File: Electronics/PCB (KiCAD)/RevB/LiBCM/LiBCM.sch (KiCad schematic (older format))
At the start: 187 parts, among them J1 Conn_01x08, J10 Screw_Terminal_01x03, J11 Screw_Terminal_01x08, J14 Conn_01x04, J15 Conn_01x02, J2 Conn_01x08, J3 Conn_01x08, J4 Conn_02x03_Odd_Even, J5 Conn_01x08, J6 Conn_01x08, J7 Conn_01x08, J8 Screw_Terminal_01x06, J9 Screw_Terminal_01x08, M1 Fan, M2 Fan, M3 Fan, P1 OEM_BCM_Connector, P2 Conn_WallPlug_Earth, Q1 Q_NMOS_GSD, Q2 Q_NMOS_GSD, Q3 Q_NMOS_GSD, Q4 Q_NMOS_GSD, Q5 Q_NMOS_GSD, Q6 Q_NMOS_GSD, Q7 Q_NMOS_GSD, Q74 Q_NMOS_GSD, Q75 Q_PMOS_GSD, Q76 Q_NMOS_GSD, SW1 SW_Push, SW2 SW_DIP_x02, U1 AP63205WU, U2 LT1487, U3 LT1487, U4 LT1797, U5 MOC3023M, U6 SFH620A-2X007T, U7 SFH620A-2X007T, U8 EPM1210SJ, U9 H11D1SR2VM

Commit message: RevB PCB Gerbers
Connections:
- no-connect marks 16 -> 17
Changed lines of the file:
@@
 Text Label 5150 13050 0    60   ~ 0
 HLINE_JUMPER
+NoConn ~ 8800 -5250
 $EndSCHEMATC

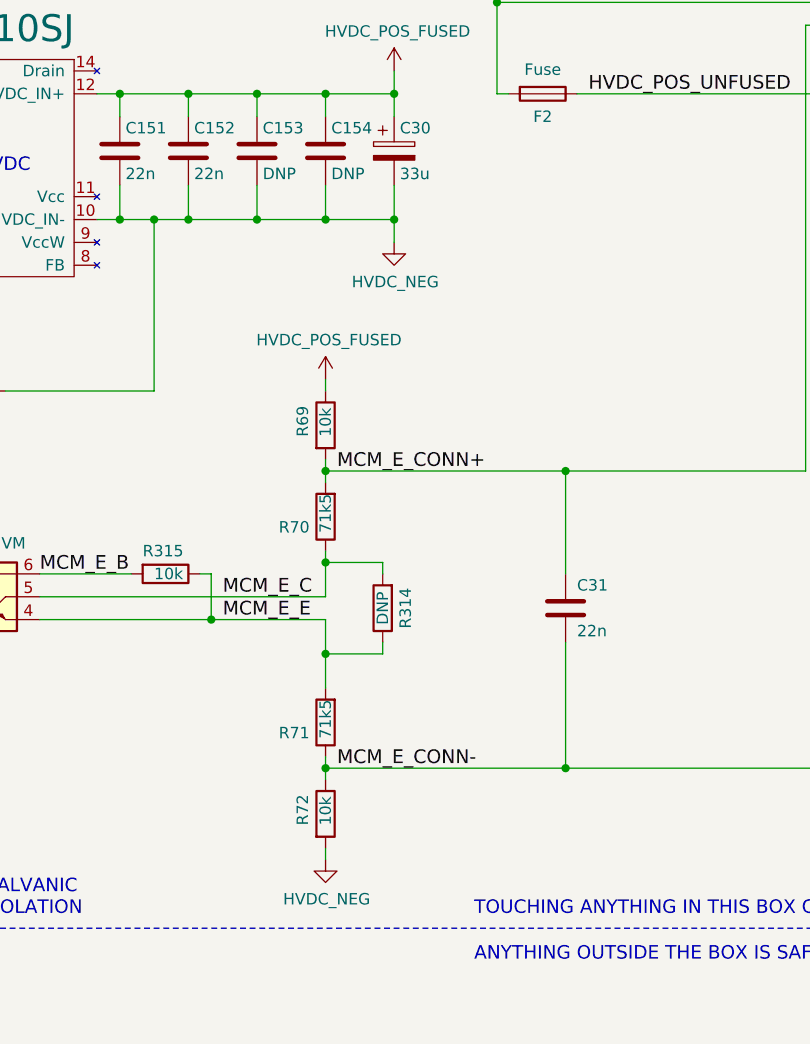
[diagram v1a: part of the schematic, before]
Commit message: Final BOM prep prior to RevB Assembly
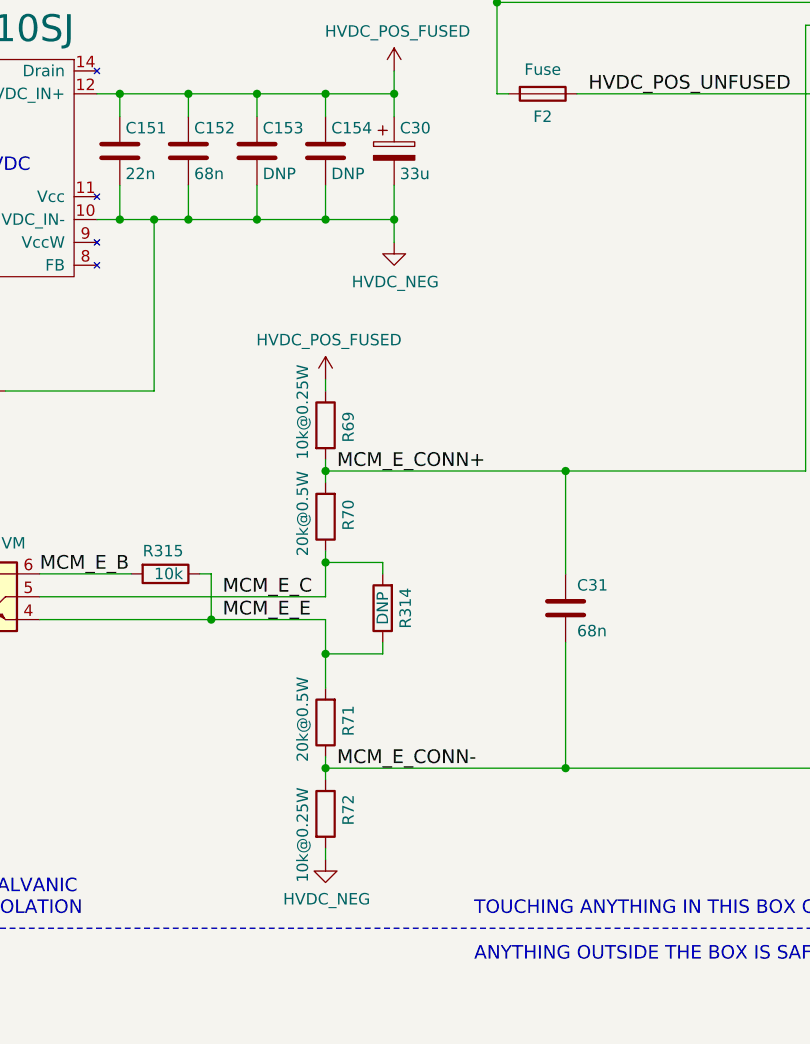
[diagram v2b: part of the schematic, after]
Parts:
- C152, C31: value 22n -> 68n
- R69, R72: value 10k -> 10k@0.25W
- R70, R71: value 71k5 -> 20k@0.5W
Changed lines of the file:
@@
 P 19150 7400
 F 0 "C31" H 19200 7300 50  0000 L CNN
-F 1 "22n" H 19200 7500 50  0000 L CNN
+F 1 "68n" H 19200 7500 50  0000 L CNN
 F 2 "Capacitor_SMD:C_1206_3216Metric" H 19188 7250 50  0001 C CNN
 F 3 "" H 19150 7400 50  0000 C CNN
@@
 U 1 1 6145179C
 P 18100 6600
-F 0 "R69" V 18000 6550 50  0000 L CNN
-F 1 "10k" V 18100 6550 50  0000 L CNN
+F 0 "R69" V 18200 6525 50  0000 L CNN
+F 1 "10k@0.25W" V 18000 6450 50  0000 L CNN
 F 2 "Resistor_SMD:R_0805_2012Metric" V 18030 6600 50  0001 C CNN
 F 3 "~" H 18100 6600 50  0001 C CNN
@@
 U 1 1 61452300
 P 18100 8300
-F 0 "R72" V 18000 8250 50  0000 L CNN
-F 1 "10k" V 18100 8250 50  0000 L CNN
+F 0 "R72" V 18200 8250 50  0000 L CNN
+F 1 "10k@0.25W" V 18000 8000 50  0000 L CNN
 F 2 "Resistor_SMD:R_0805_2012Metric" V 18030 8300 50  0001 C CNN
 F 3 "~" H 18100 8300 50  0001 C CNN
@@
 U 1 1 6150E071
 P 18100 7000
-F 0 "R70" H 18170 7046 50  0000 L CNN
-F 1 "71k5" V 18100 6900 50  0000 L CNN
+F 0 "R70" V 18000 6925 50  0000 L CNN
+F 1 "20k@0.5W" V 18200 6800 50  0000 L CNN
 F 2 "Resistor_SMD:R_0805_2012Metric" V 18030 7000 50  0001 C CNN
 F 3 "~" H 18100 7000 50  0001 C CNN
@@
 U 1 1 614525D7
 P 18100 7900
-F 0 "R71" H 18170 7946 50  0000 L CNN
-F 1 "71k5" V 18100 7800 50  0000 L CNN
+F 0 "R71" V 18000 7825 50  0000 L CNN
+F 1 "20k@0.5W" V 18200 7700 50  0000 L CNN
 F 2 "Resistor_SMD:R_0805_2012Metric" V 18030 7900 50  0001 C CNN
 F 3 "~" H 18100 7900 50  0001 C CNN
@@
 P 17500 5400
 F 0 "C152" H 17525 5300 50  0000 L CNN
-F 1 "22n" H 17525 5500 50  0000 L CNN
+F 1 "68n" H 17525 5500 50  0000 L CNN
 F 2 "Capacitor_SMD:C_1206_3216Metric" H 17538 5250 50  0001 C CNN
 F 3 "" H 17500 5400 50  0000 C CNN
